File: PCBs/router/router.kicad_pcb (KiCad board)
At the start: 2 copper layers, 95.3 x 110 mm, 37 parts, among them J1 Conn_01x06_Male, J10 Conn_01x06_Male, J11 Conn_01x06_Male, J12 Conn_01x06_Male, J13 Conn_01x06_Male, J14 Conn_01x06_Male, J15 Conn_01x06_Male, J2 Conn_01x06_Male, J3 Conn_01x06_Male, J4 Conn_01x06_Male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

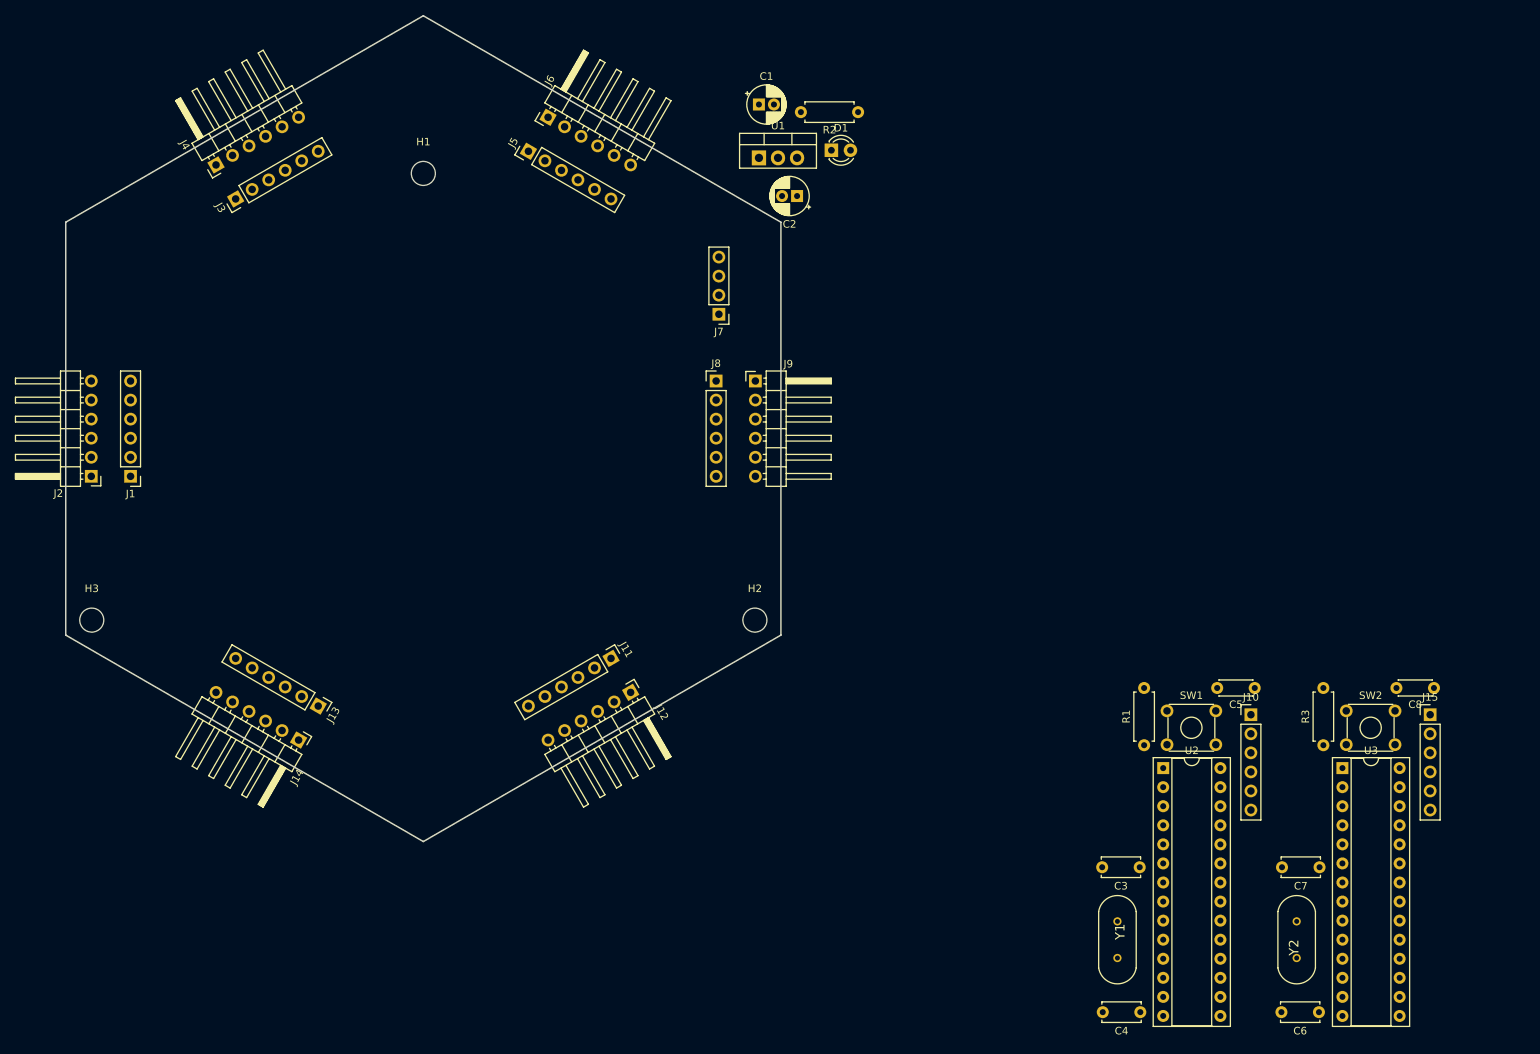
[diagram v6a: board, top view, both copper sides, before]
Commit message: place other components
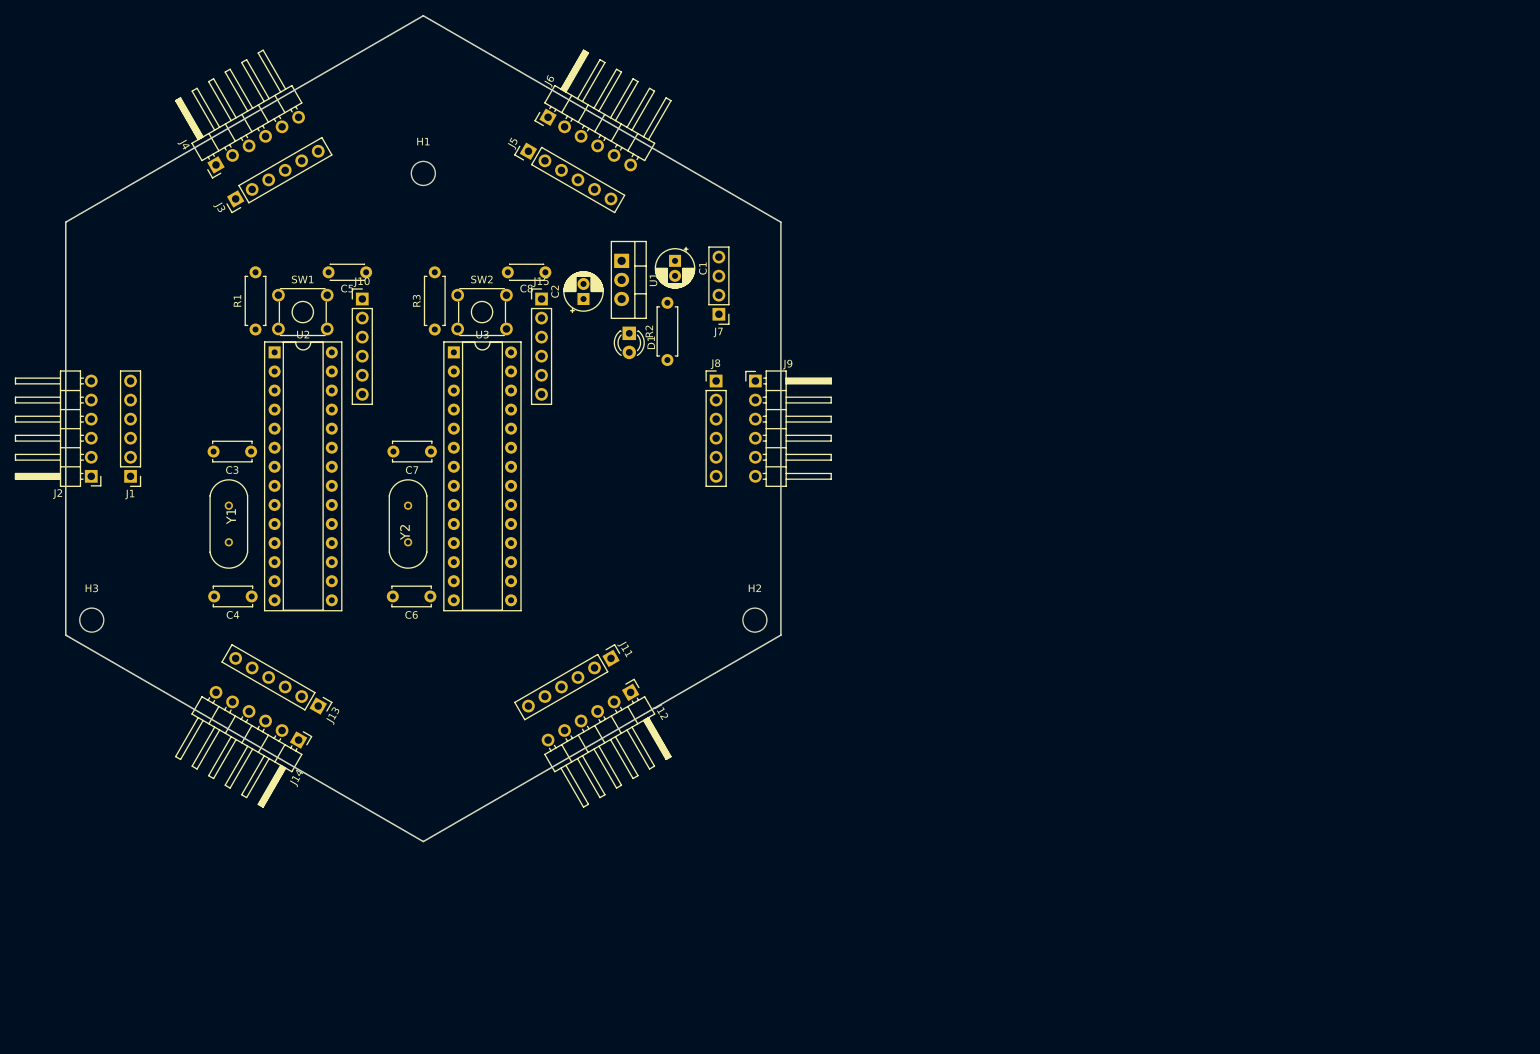
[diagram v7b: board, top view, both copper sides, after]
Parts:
- moved J10 130.7 mm to (144.3, 84.3)
- moved Y2 130.7 mm to (150.4, 114.3)
- moved C3 130.7 mm to (129.5, 104.6)
- moved C4 130.7 mm to (129.5, 124.0)
- moved C5 130.7 mm to (144.8, 80.8)
- moved J15 130.7 mm to (168.1, 84.3)
- moved R1 130.7 mm to (130.0, 88.4)
- moved R3 130.7 mm to (153.9, 88.4)
- moved SW1 130.7 mm to (133.1, 83.8)
- moved SW2 130.7 mm to (157.0, 83.8)
- moved U2 130.7 mm to (132.6, 91.4)
- moved Y1 130.7 mm to (126.5, 114.3)
- moved C6 130.7 mm to (153.3, 124.0)
- moved C7 130.7 mm to (153.4, 104.6)
- moved C8 130.7 mm to (168.7, 80.8)
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
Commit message: power bus
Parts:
- moved R2 28.5 mm to (183.9, 120.9)
- moved C2 28.5 mm to (172.7, 112.8)
- moved D1 28.5 mm to (178.8, 117.3)
- moved U1 28.5 mm to (177.8, 107.7)
- moved C1 27.5 mm to (184.9, 106.7)
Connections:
- J7 pad 1: GND -> +9V
- J7 pad 4: +9V -> GND
- U2 pad 23: Net-(J7-Pad2) -> Net-(J7-Pad3)
- U2 pad 24: Net-(J7-Pad3) -> Net-(J7-Pad2)
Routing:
- net GND: track 0.00 -> 353.8 mm
- net +9V: track 0.00 -> 307.1 mm
